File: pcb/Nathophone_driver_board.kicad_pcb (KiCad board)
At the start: 4 copper layers, 160 x 110 mm, 239 parts, among them J1 PJ-063AH, J10 TERM BLOCK, J11 TERM BLOCK, J12 TERM BLOCK, J13 TERM BLOCK, J2 54202-S0806ALF, J3 Conn_01x30, J4 54202-S0806ALF, J5 54202-S0806ALF, J6 54202-S0806ALF, J7 TERM BLOCK, J8 54202-S0806ALF, J9 TERM BLOCK, Q1 2N7002H, Q10 BSS84, Q11 BSS84, Q12 BSS84, Q13 BSS84, Q2 2N7002H, Q3 FDN340P, Q4 FQD11P06TM, Q5 FDN340P, Q6 2N7002H, Q7 2N7002H, Q8 BSS84, Q9 BSS84, SW1 1-1571986-1, SW2 PTS645SM43SMTR92 LFS, SW3 DS04-254-2-01BK-SMT, U1 LT8650SEV_PBF, U2 SPX3819M5-L-3-3, U3 74LVC2G07, U4 TAS5720MRSMR, U5 TAS5720MRSMR, U6 TAS5720MRSMR, U7 TAS5720MRSMR, U8 TAS5720MRSMR, U9 TAS5720MRSMR

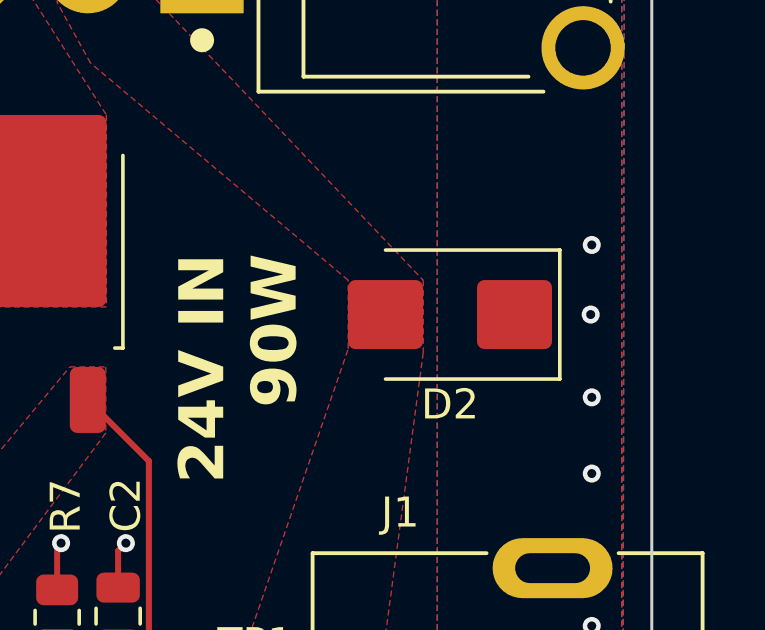
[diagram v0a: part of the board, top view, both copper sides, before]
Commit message: CORRECTED TVS Diode polarisation
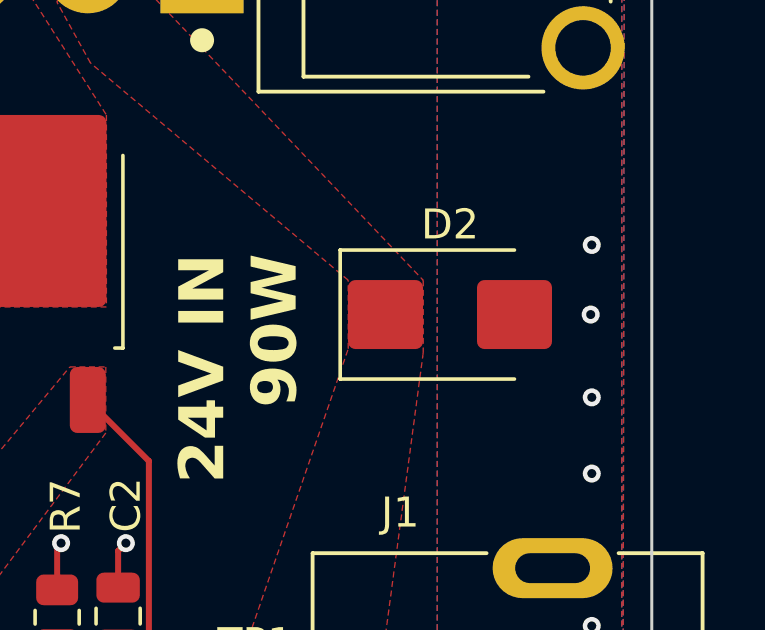
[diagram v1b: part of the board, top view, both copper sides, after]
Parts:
- D2: value CP-063AH-ND -> TPSMB2616CA
- turned D2 to 0 degrees
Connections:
- D2 pad 1: GND -> Net-(D2-K)
- D2 pad 2: Net-(D2-A2) -> GND
- J1 pad 1: Net-(D2-A2) -> Net-(D2-K)
- SW1 pad 2: Net-(D2-A2) -> Net-(D2-K)
- TP1 pad 1: Net-(D2-A2) -> Net-(D2-K)
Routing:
- added copper zone on F.Cu, net Net-(D2-K)
- removed copper zone on F.Cu, net Net-(D2-A2)
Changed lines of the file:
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@@
 		(tenting front back)
 		(pcbplotparams
-			(layerselection 0x00000000_00000000_55555555_55555575)
-			(plot_on_all_layers_selection 0x00000000_00000000_00000000_02000000)
+			(layerselection 0x00000000_00000000_55555555_55555520)
+			(plot_on_all_layers_selection 0x00000000_00000000_00000000_02000002)
 			(disableapertmacros no)
 			(usegerberextensions no)
@@
 			(dashed_line_gap_ratio 3.000000)
 			(svgprecision 4)
-			(plotframeref no)
+			(plotframeref yes)
 			(mode 1)
 			(useauxorigin no)
@@
 			(psnegative no)
 			(psa4output no)
-			(plot_black_and_white no)
-			(sketchpadsonfab no)
-			(plotpadnumbers no)
+			(plot_black_and_white yes)
+			(sketchpadsonfab yes)
+			(plotpadnumbers yes)
 			(hidednponfab no)
 			(sketchdnponfab yes)
@@
 	(net 55 "Net-(D1-A)")
 	(net 56 "Net-(D1-K)")
-	(net 57 "Net-(D2-A2)")
+	(net 57 "Net-(D2-K)")
 	(net 58 "+5V_ext")
 	(net 59 "Net-(D4-A)")
@@
 			(layers "*.Cu" "*.Mask")
 			(remove_unused_layers no)
-			(net 57 "Net-(D2-A2)")
+			(net 57 "Net-(D2-K)")
 			(pintype "passive")
 			(solder_mask_margin 0.102)
@@
 			(layers "*.Cu" "*.Mask")
 			(remove_unused_layers no)
-			(net 57 "Net-(D2-A2)")
+			(net 57 "Net-(D2-K)")
 			(pintype "passive")
 			(solder_mask_margin 0.102)
@@
 			(size 2 2)
 			(layers "F.Cu" "F.Mask")
-			(net 57 "Net-(D2-A2)")
+			(net 57 "Net-(D2-K)")
 			(pinfunction "1")
 			(pintype "passive")
@@
 		(placed yes)
 		(layer "F.Cu")
-		(at 215.274 71.12 180)
+		(at 215.274 71.12)
 		(descr "Diode SMB (DO-214AA)")
 		(tags "Diode SMB (DO-214AA)")
@@
 			)
 		)
-		(property "Value" "CP-063AH-ND"
+		(property "Value" "TPSMB2616CA"
 			(at 0 3.1 0)
 			(layer "F.Fab")
@@
 		)
 		(property "Datasheet" "https://www.littelfuse.com/assetdocs/tvs-diode-tpsmb-datasheet?assetguid=E7A196A8-A225-4724-AB76-7C22E0D48557"
-			(at 0 0 180)
+			(at 0 0 0)
 			(unlocked yes)
 			(layer "F.Fab")
@@
 		)
 		(property "Description" "Bidirectional transient-voltage-suppression diode"
-			(at 0 0 180)
+			(at 0 0 0)
 			(unlocked yes)
 			(layer "F.Fab")
@@
 		)
 		(property "DigiKey_PartNo" "18-TPSMB2616CATR-ND"
-			(at 0 0 180)
+			(at 0 0 0)
 			(unlocked yes)
 			(layer "F.Fab")
@@
 		)
 		(property "Key Info" "39,5V max. Clamp / 14,3A peak"
-			(at 0 0 180)
+			(at 0 0 0)
 			(unlocked yes)
 			(layer "F.Fab")
@@
 		)
 		(property "MPN" "TPSMB2616CA"
-			(at 0 0 180)
+			(at 0 0 0)
 			(unlocked yes)
 			(layer "F.Fab")
@@
 		(attr smd)
 		(fp_line
-			(start -3.66 2.15)
-			(end 2.15 2.15)
+			(start -3.66 -2.15)
+			(end -3.66 2.15)
 			(stroke
 				(width 0.12)
@@
 		)
 		(fp_line
-			(start -3.66 -2.15)
-			(end -3.66 2.15)
+			(start -3.66 2.15)
+			(end 2.15 2.15)
 			(stroke
 				(width 0.12)
@@
 		)
 		(fp_line
-			(start 3.65 2.25)
-			(end -3.65 2.25)
+			(start -3.65 -2.25)
+			(end 3.65 -2.25)
 			(stroke
 				(width 0.05)
@@
 		)
 		(fp_line
-			(start 3.65 -2.25)
-			(end 3.65 2.25)
+			(start -3.65 2.25)
+			(end -3.65 -2.25)
 			(stroke
 				(width 0.05)
@@
 		)
 		(fp_line
-			(start -3.65 2.25)
-			(end -3.65 -2.25)
+			(start 3.65 -2.25)
+			(end 3.65 2.25)
 			(stroke
 				(width 0.05)
@@
 		)
 		(fp_line
-			(start -3.65 -2.25)
-			(end 3.65 -2.25)
+			(start 3.65 2.25)
+			(end -3.65 2.25)
 			(stroke
 				(width 0.05)
@@
 		)
 		(fp_line
-			(start 2.3 2)
-			(end -2.3 2)
+			(start -2.3 2)
+			(end -2.3 -2)
 			(stroke
 				(width 0.1)
@@
 		)
 		(fp_line
-			(start 2.3 -2)
-			(end 2.3 2)
+			(start -0.64944 -0.79908)
+			(end -0.64944 0.80112)
 			(stroke
 				(width 0.1)
@@
 		)
 		(fp_line
-			(start 2.3 -2)
-			(end -2.3 -2)
+			(start -0.64944 0.00102)
+			(end -1.55114 0.00102)
 			(stroke
 				(width 0.1)
@@
 		)
 		(fp_line
-			(start 0.50118 0.75032)
+			(start -0.64944 0.00102)
 			(end 0.50118 -0.79908)
 			(stroke
@@
 		)
 		(fp_line
-			(start 0.50118 0.00102)
-			(end 1.4994 0.00102)
+			(start -0.64944 0.00102)
+			(end 0.50118 0.75032)
 			(stroke
 				(width 0.1)
@@
 		)
 		(fp_line
-			(start -0.64944 0.00102)
-			(end 0.50118 0.75032)
+			(start 0.50118 0.00102)
+			(end 1.4994 0.00102)
 			(stroke
 				(width 0.1)
@@
 		)
 		(fp_line
-			(start -0.64944 0.00102)
+			(start 0.50118 0.75032)
 			(end 0.50118 -0.79908)
 			(stroke
@@
 		)
 		(fp_line
-			(start -0.64944 0.00102)
-			(end -1.55114 0.00102)
+			(start 2.3 -2)
+			(end -2.3 -2)
 			(stroke
 				(width 0.1)
@@
 		)
 		(fp_line
-			(start -0.64944 -0.79908)
-			(end -0.64944 0.80112)
+			(start 2.3 -2)
+			(end 2.3 2)
 			(stroke
 				(width 0.1)
@@
 		)
 		(fp_line
-			(start -2.3 2)
-			(end -2.3 -2)
+			(start 2.3 2)
+			(end -2.3 2)
 			(stroke
 				(width 0.1)
@@
 		)
 		(pad "1" smd roundrect
-			(at -2.15 0 180)
+			(at -2.15 0)
 			(size 2.5 2.3)
 			(layers "F.Cu" "F.Mask" "F.Paste")
 			(roundrect_rratio 0.1086956522)
-			(net 1 "GND")
-			(pinfunction "A1")
+			(net 57 "Net-(D2-K)")
+			(pinfunction "K")
 			(pintype "passive")
 		)
 		(pad "2" smd roundrect
-			(at 2.15 0 180)
+			(at 2.15 0)
 			(size 2.5 2.3)
 			(layers "F.Cu" "F.Mask" "F.Paste")
 			(roundrect_rratio 0.1086956522)
-			(net 57 "Net-(D2-A2)")
-			(pinfunction "A2")
+			(net 1 "GND")
+			(pinfunction "A")
 			(pintype "passive")
 		)
@@
 	(zone
 		(net 57)
-		(net_name "Net-(D2-A2)")
+		(net_name "Net-(D2-K)")
 		(locked yes)
 		(layer "F.Cu")
